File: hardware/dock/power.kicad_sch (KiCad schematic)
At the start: 0 parts

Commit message: Dock schematic: review fixes, Pico 2/XIAO socket+pogo mounting
- Cross HID UART TX/RX; split ROLE_STRAP per endpoint
- VBUS sense (GP4) and USB-C CC current sensing (GP26/27) on HID endpoints
- Pogo +5V via TPS2552 enabled by DET, TPD4E1U06 ESD + 1k on pogo lines
- 2x100uF bulk on SYS_5V and keyboard VBUS; 100k EN pull-down
- Remove TPS62162 rail: XIAO from 5V, pull-ups on module 3V3 rails
- Socketed Pico 2 / XIAO footprints with P50-B1 probe holes for USB+SWD
- XIAO SWD header J8; RP2350 reset control of HID/BLE endpoints
- DESIGN.md: UART allocation, power budget, mounting, reset control
- Add .gitignore, custom libraries and datasheets

Co-Authored-By: Claude Opus 5.5 <noreply@anthropic.com>
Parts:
- added C13, C14: 100uF, Capacitor_SMD:CP_Elec_6.3x7.7, symbol Device:C_Polarized
- added C3: 1µF, Capacitor_SMD:C_0805_2012Metric_Pad1.18x1.45mm_HandSolder, symbol Device:C
- added C8, C9: 1uF, Capacitor_SMD:C_0805_2012Metric_Pad1.18x1.45mm_HandSolder, symbol Device:C
- added R1: 300K, Resistor_SMD:R_0805_2012Metric_Pad1.20x1.40mm_HandSolder, symbol Device:R
- added R2: 100K, Resistor_SMD:R_0805_2012Metric_Pad1.20x1.40mm_HandSolder, symbol Device:R
- added R3: 10k, Resistor_SMD:R_0805_2012Metric_Pad1.20x1.40mm_HandSolder, symbol Device:R
- added U1: TPS2116DRL, Package_TO_SOT_SMD:SOT-583-8, symbol Power_Management:TPS2116DRL
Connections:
- new net: R1.1, R2.2, U1.4 (PR1)
- new net GND: C13.2, C14.2, C3.1, C8.2, C9.1, R2.1, U1.1 (GND)
- new net HOST_3V3: R3.1
- new net MUX_STATUS: R3.2, U1.8 (ST)
- new net PERSONAL_VBUS: C9.2, R1.2, U1.3 (VIN1), U1.5 (MODE)
- new net SYS_5V: C13.1, C14.1, C3.2, U1.2 (VOUT), U1.7 (VOUT)
- new net WORK_VBUS: C8.1, U1.6 (VIN2)

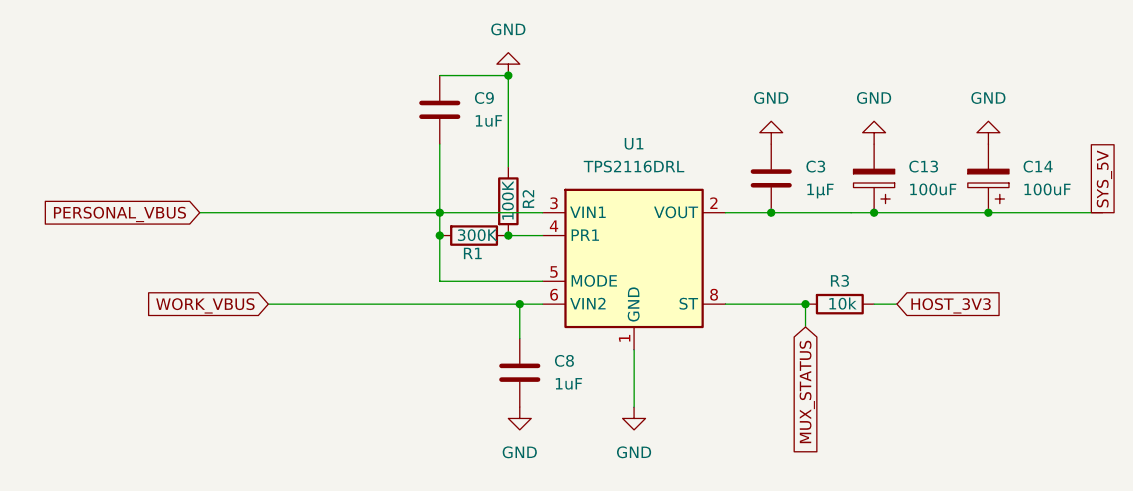
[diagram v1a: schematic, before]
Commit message: Net classes, project lib tables, docs and datasheets; PCB synced
- Rename USB pairs to *_D_P/*_D_N; add Power and USB net classes
- Project-relative fp-lib-table and new sym-lib-table
- Pico values set to "Raspberry Pi Pico 2"; J1 symbol synced with library
- DESIGN.md/README: Pico 2 x3 + XIAO modules, TPS2116, pogo switch/ESD,
  VBUS/CC sensing, SWD pinout, resolved and open items
- Add TPS2552/2553, TPD2EUSB30 and P50 probe datasheets
- PCB updated from schematic (F8)

Co-Authored-By: Claude Opus 5.5 <noreply@anthropic.com>
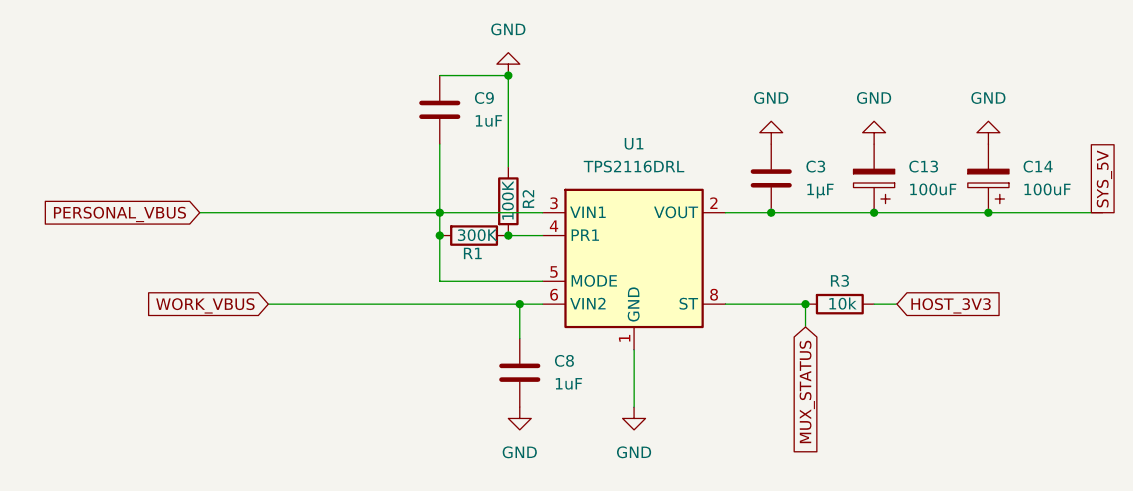
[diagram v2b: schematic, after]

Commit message: TPS2116: hand-solder SOT-583-8 footprint with extended pads
Pads 1.2 x 0.3 mm (inner edge unchanged, outer edge +0.53 mm) so the
0.5 mm-pitch DRL package can be soldered with an iron. TPS2116 is only
available in DRL, so the package itself cannot be enlarged.

Co-Authored-By: Claude Opus 5.5 <noreply@anthropic.com>
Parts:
- U1: footprint Package_TO_SOT_SMD:SOT-583-8 -> dock:SOT-583-8_HandSolder
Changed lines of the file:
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@@
 			)
 		)
-		(property "Footprint" "Package_TO_SOT_SMD:SOT-583-8"
+		(property "Footprint" "dock:SOT-583-8_HandSolder"
 			(at 104.14 118.872 0)
 			(hide yes)
